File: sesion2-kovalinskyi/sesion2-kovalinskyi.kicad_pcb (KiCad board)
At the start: 2 copper layers, 63.5 x 28 mm, 10 parts, among them J1 Screw_Terminal_01x02, J2 Conn_01x06_Pin, U1 LD1117S33TR_SOT223, U2 ATmega328P-AU

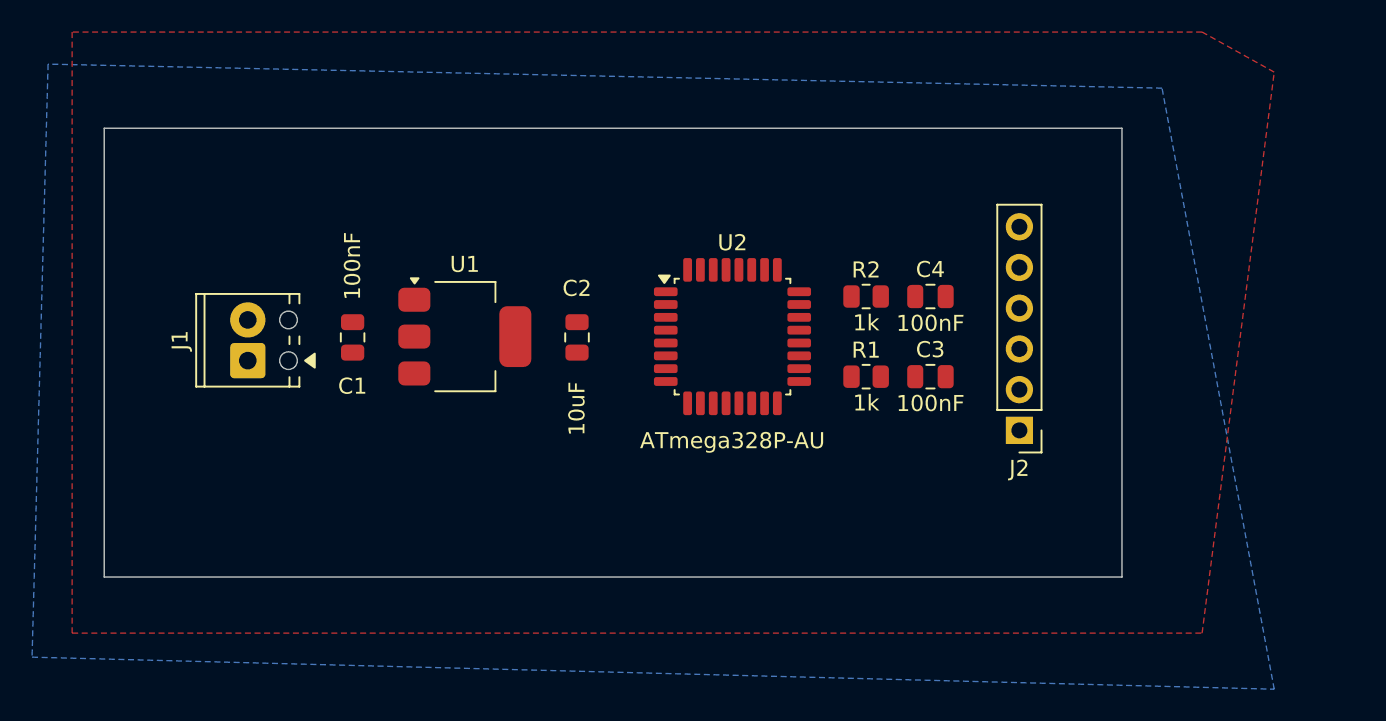
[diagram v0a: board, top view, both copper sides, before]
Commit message: Avance en layout y enrutado preliminar
- Enrutadas señales de datos, filtros y componentes pasivos.
- Implementados condensadores de desacoplo y test points (VIN, 3V3, GND).

Pendiente:
- Corregir asignación de ancho para pistas de alimentación (+3V3 a 0,5 mm).
- Validar conexiones a GND y cosido de vías con el plano inferior (B.Cu).
- Ejecutar DRC final y recálculo de zonas de relleno.
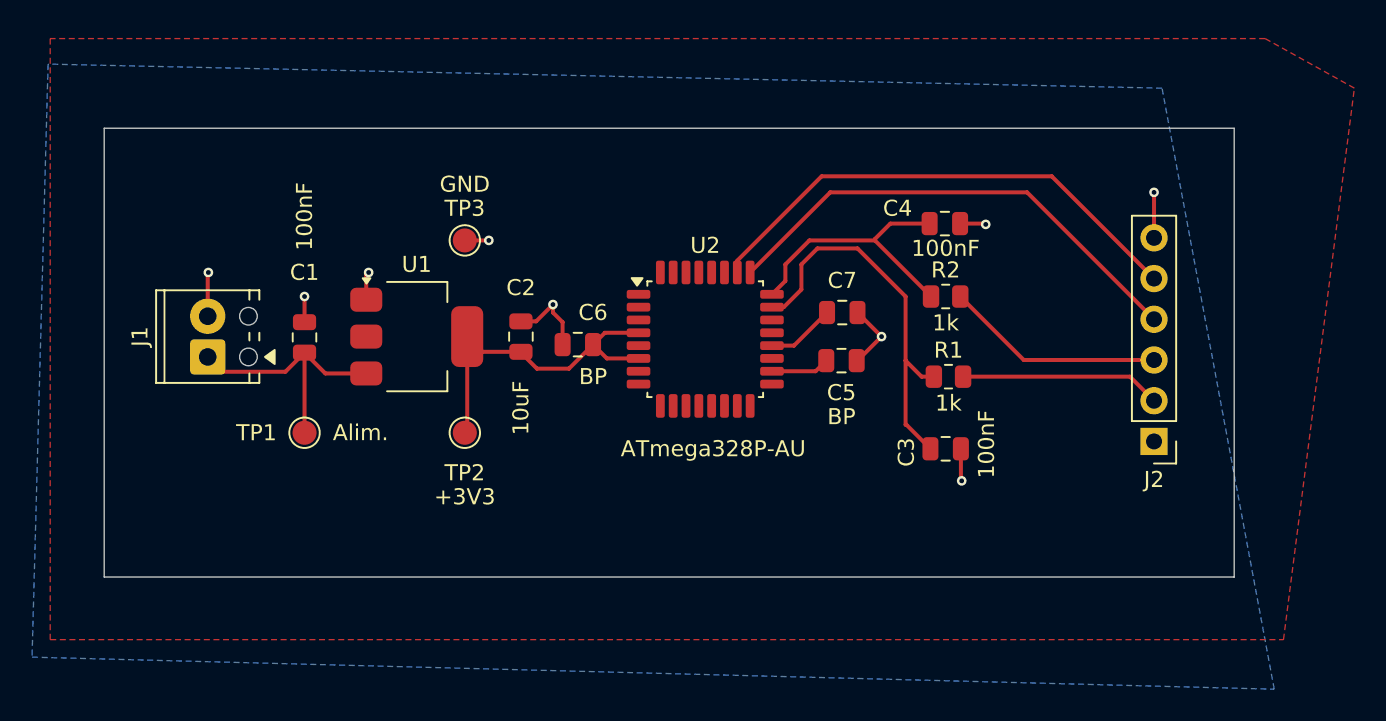
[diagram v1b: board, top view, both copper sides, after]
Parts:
- added C5: BP, Capacitor_SMD:C_0805_2012Metric, F.Cu at (81.5, 65.0)
- added C6: BP, Capacitor_SMD:C_0805_2012Metric, F.Cu at (65.0, 64.0)
- added C7: 100nF, Capacitor_SMD:C_0805_2012Metric, F.Cu at (81.5, 62.0)
- added TP1: Alim., TestPoint:TestPoint_Pad_D1.5mm, F.Cu at (48.0, 69.5)
- added TP2: +3V3, TestPoint:TestPoint_Pad_D1.5mm, F.Cu at (58.0, 69.5)
- added TP3: TestPoint, TestPoint:TestPoint_Pad_D1.5mm, F.Cu at (58.0, 57.5)
- moved J2 8.43 mm to (101.0, 70.0)
- moved R1 5.14 mm to (88.2, 66.0)
- moved R2 4.96 mm to (88.0, 61.0)
- moved C4 4.64 mm to (88.0, 56.5)
- moved C3 4.60 mm to (88.0, 70.5)
- moved C2 3.50 mm to (61.5, 63.5)
- moved C1 3.00 mm to (48.0, 63.5)
- moved U1 3.00 mm to (55.0, 63.5)
- moved J1 2.51 mm to (42.0, 64.8)
- moved U2 1.71 mm to (73.0, 63.7)
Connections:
- U2 pad 20: unconnected-(U2-AREF-Pad20) -> Net-(U2-AREF)
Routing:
- net Net-(J2-Pin_5): track 0.00 -> 31.6 mm
- net Net-(J2-Pin_4): track 0.00 -> 30.6 mm
- net /alimentacion/+3V3: track 0.00 -> 25.4 mm
- net Net-(U2-PC0): track 0.00 -> 24.4 mm
- net /alimentacion/GND: track 0.00 -> 24.0 mm, vias 0 -> 9
- net Net-(U2-PC1): track 0.00 -> 17.3 mm
- net Net-(J1-Pin_1): track 0.00 -> 16.3 mm
- net Net-(J2-Pin_3): track 0.00 -> 13.7 mm
- net Net-(J2-Pin_2): track 0.00 -> 12.5 mm
- net Net-(U2-AREF): track 0.00 -> 4.29 mm
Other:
- board size 63.5 x 28 mm -> 70.5 x 28 mm
- board text added: "GND"

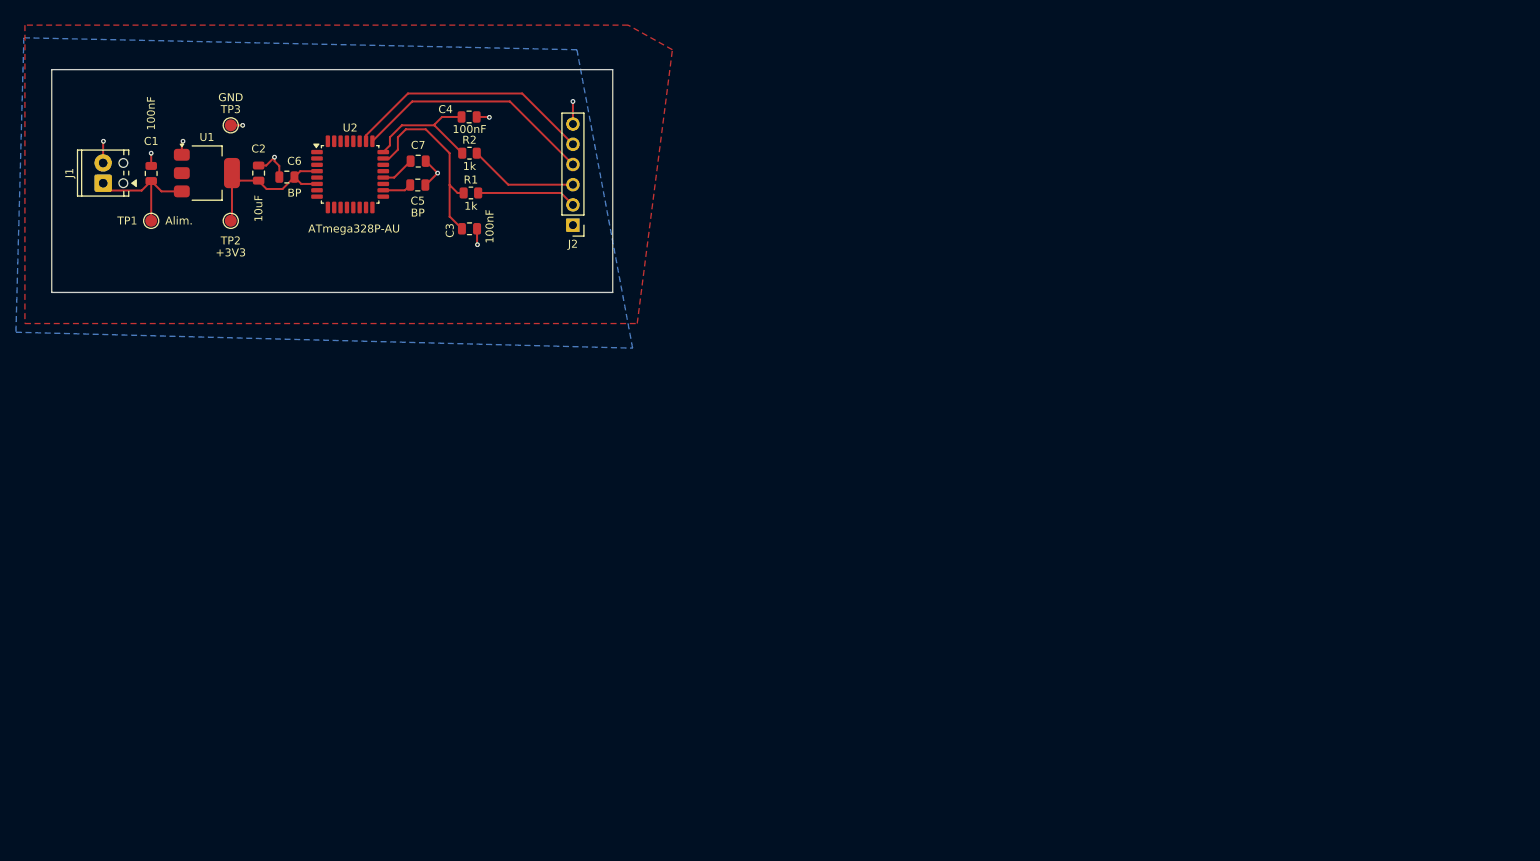
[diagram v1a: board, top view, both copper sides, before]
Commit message: Layout FINAL (Tarea - Sesión 3)
- Configuración de Net Classes (GND, POWER, SIGNAL) con anchos de pista (>=0.25 mm) y clearance (0.2 mm) según especificaciones.
- Optimización de layout: flujo lógico de señal/alimentación, condensadores de desacoplo junto a sus pines y conectores en los extremos.
- Ruteo eficiente minimizando vías y conectando planos de GND y +3V3.
- Verificación DRC superada con éxito (0 errores, 0 avisos).
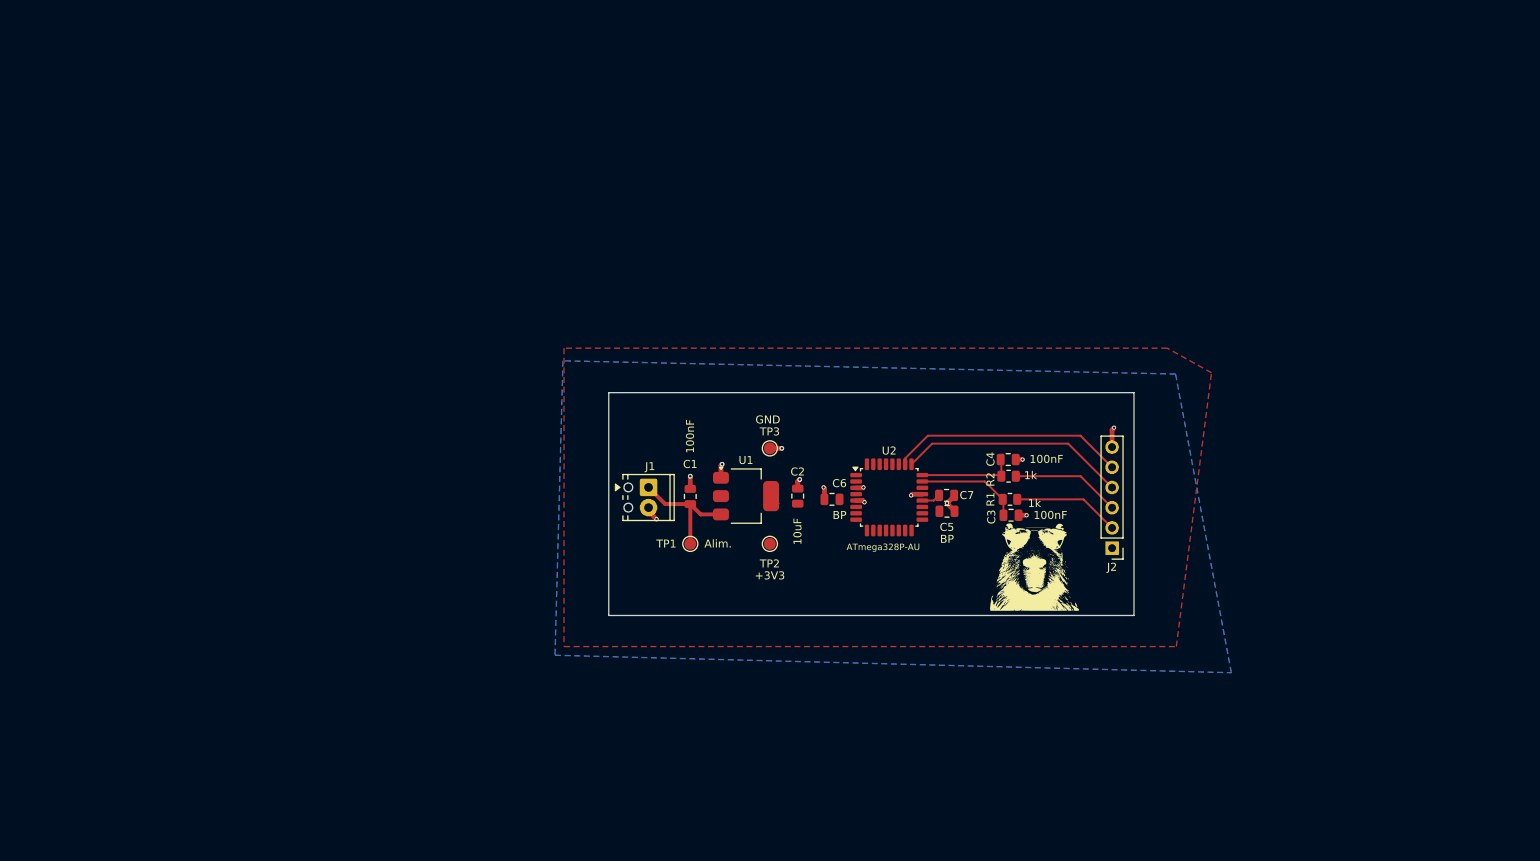
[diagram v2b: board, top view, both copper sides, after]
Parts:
- added G***: LOGO, LOGO, F.Cu at (159.0, 112.5)
- moved C4 80.3 mm to (155.7, 99.5)
- moved C6 79.6 mm to (133.6, 104.5)
- moved C1 79.0 mm to (115.7, 104.1)
- moved C2 79.0 mm to (129.2, 104.1)
- moved J2 79.0 mm to (168.7, 110.6)
- moved R2 79.0 mm to (155.7, 101.6)
- moved TP1 79.0 mm to (115.7, 110.1)
- moved TP2 79.0 mm to (125.7, 110.1)
- moved TP3 79.0 mm to (125.7, 98.1)
- moved U1 79.0 mm to (122.7, 104.1)
- moved U2 79.0 mm to (140.7, 104.3)
- moved C7 78.6 mm to (147.9, 104.0)
- moved J1 78.5 mm to (110.5, 103.0), turned to -90 degrees
- moved C5 78.1 mm to (148.0, 106.0)
- moved R1 77.9 mm to (155.9, 104.5)
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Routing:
- net /alimentacion/+3V3: track 25.4 -> 2.11 mm
- net Net-(U2-PC0): track 24.4 -> 13.1 mm
- net Net-(U2-PC1): track 17.3 -> 12.1 mm
- net /alimentacion/GND: track 24.0 -> 20.4 mm, vias 9 -> 13
- net Net-(J2-Pin_5): track 31.6 -> 29.6 mm
- net Net-(J2-Pin_4): track 30.6 -> 28.6 mm
- net Net-(U2-AREF): track 4.29 -> 2.36 mm
- net Net-(J2-Pin_2): track 12.5 -> 13.4 mm
- net Net-(J1-Pin_1): track 16.3 -> 15.6 mm
- added copper zone on B.Cu, net /alimentacion/GND
- removed copper zone on B.Cu, net /alimentacion/+3V3
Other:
- board size 70.5 x 28 mm -> 66 x 28 mm

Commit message: Calculo de impedancia y enrutado SPI e I2C
- I2C enrutado en Capa 3 (Stripline) con meandros (regla 3W) y desacoplo C8 pegado a los pines.
- SPI en Capa 1 con ajuste de longitud en SCK, MOSI y MISO (~25,35 mm) y puente en Capa 3 para SPI_CS.
- Validada la integridad de señal en los buses; líneas de datos libres de errores DRC.
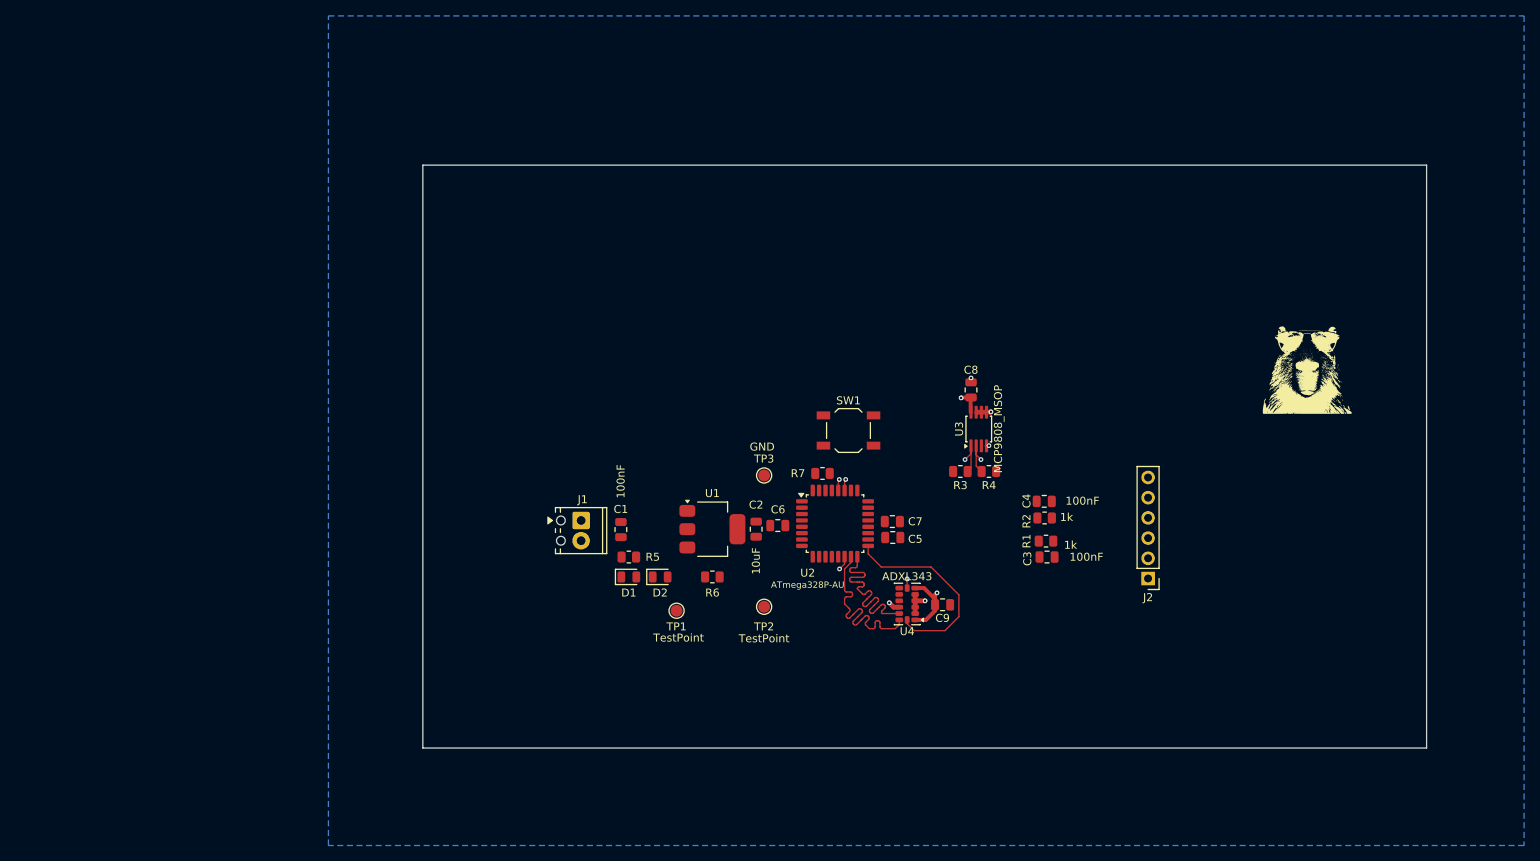
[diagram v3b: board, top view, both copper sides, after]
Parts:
- added C8: 100nF, Capacitor_SMD:C_0805_2012Metric, F.Cu at (151.0, 90.8)
- added C9: 100nF, Capacitor_SMD:C_0805_2012Metric, F.Cu at (147.4, 117.8)
- added D1: LED_AZUL, LED_SMD:LED_0805_2012Metric, F.Cu at (108.0, 114.2)
- added D2: LED_VERDE, LED_SMD:LED_0805_2012Metric, F.Cu at (112.0, 114.2)
- added R3: 4.7k, Resistor_SMD:R_0805_2012Metric, F.Cu at (149.7, 101.0)
- added R4: 4.7k, Resistor_SMD:R_0805_2012Metric, F.Cu at (153.3, 101.0)
- added R5: 1k, Resistor_SMD:R_0805_2012Metric, F.Cu at (108.0, 111.8)
- added R6: 470, Resistor_SMD:R_0805_2012Metric, F.Cu at (118.5, 114.2)
- added R7: 10k, Resistor_SMD:R_0805_2012Metric, F.Cu at (132.4, 101.2)
- added SW1: SW_Push, Button_Switch_SMD:SW_SPST_TL3342, F.Cu at (135.6, 95.8)
- added U3: MCP9808_MSOP, Package_SO:MSOP-8_3x3mm_P0.65mm, F.Cu at (152.0, 95.7)
- added U4: ADXL343, Package_LGA:LGA-14_3x5mm_P0.8mm_LayoutBorder1x6y, F.Cu at (143.0, 117.7)
- C5, C6: value BP -> 100nF
- TP1: value Alim. -> TestPoint
- TP2: value +3V3 -> TestPoint
- moved G*** 42.3 mm to (193.3, 87.8)
- moved C1 9.66 mm to (107.0, 108.3)
- moved J1 9.44 mm to (102.0, 107.2)
- moved TP1 8.58 mm to (114.0, 118.5)
- moved TP2 7.94 mm to (125.0, 118.0)
- moved C6 7.57 mm to (126.7, 107.8)
- moved C5 7.57 mm to (141.2, 109.3)
- moved C7 7.57 mm to (141.1, 107.3)
- moved U2 7.57 mm to (133.9, 107.5)
- moved C4 6.93 mm to (160.2, 104.8)
- moved C3 6.93 mm to (160.6, 111.8)
- moved R1 6.93 mm to (160.4, 109.8)
- moved R2 6.93 mm to (160.3, 106.8)
- moved C2 6.68 mm to (124.0, 108.2)
- moved U1 5.93 mm to (118.5, 108.2)
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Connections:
- U2 pad 14: unconnected-(U2-PB2-Pad14) -> /microcontrolador/SPI_CS
- U2 pad 15: unconnected-(U2-PB3-Pad15) -> /microcontrolador/SPI_MOSI
- U2 pad 16: unconnected-(U2-PB4-Pad16) -> /microcontrolador/SPI_MISO
- U2 pad 17: unconnected-(U2-PB5-Pad17) -> /microcontrolador/SPI_SCK
- U2 pad 27: unconnected-(U2-PC4-Pad27) -> /microcontrolador/SDA
- U2 pad 28: unconnected-(U2-PC5-Pad28) -> /microcontrolador/SCL
- U2 pad 29: unconnected-(U2-~{RESET}/PC6-Pad29) -> Net-(U2-~{RESET}/PC6)
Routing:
- net Net-(J2-Pin_5): track 29.6 -> 0.00 mm
- net Net-(J2-Pin_4): track 28.6 -> 0.00 mm
- net /microcontrolador/SDA: track 0.00 -> 26.3 mm, vias 0 -> 2
- net /microcontrolador/SCL: track 0.00 -> 26.2 mm, vias 0 -> 2
- net /microcontrolador/SPI_SCK: track 0.00 -> 25.3 mm
- net /microcontrolador/SPI_MOSI: track 0.00 -> 25.2 mm
- net /microcontrolador/SPI_MISO: track 0.00 -> 25.1 mm
- net Net-(J1-Pin_1): track 15.6 -> 0.00 mm
- net Net-(J2-Pin_3): track 13.7 -> 0.00 mm
- net Net-(J2-Pin_2): track 13.4 -> 0.00 mm
- net /alimentacion/GND: track 20.4 -> 7.26 mm, vias 13 -> 5
- net Net-(U2-PC0): track 13.1 -> 0.00 mm
- net Net-(U2-PC1): track 12.1 -> 0.00 mm
- net /microcontrolador/SPI_CS: track 0.00 -> 12.0 mm, vias 0 -> 2
- net /alimentacion/+3V3: track 2.11 -> 12.3 mm, vias 0 -> 2
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- added copper zone on B.Cu, net /alimentacion/+3V3
- added copper zone on In1.Cu, net /alimentacion/GND
- removed copper zone on F.Cu, net /alimentacion/+3V3
- removed copper zone on B.Cu, net /alimentacion/GND
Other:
- board size 66 x 28 mm -> 126.1 x 73.2 mm
- copper layers 2 -> 4
